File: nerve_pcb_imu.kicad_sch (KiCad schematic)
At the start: 15 parts, among them Y3 32k768

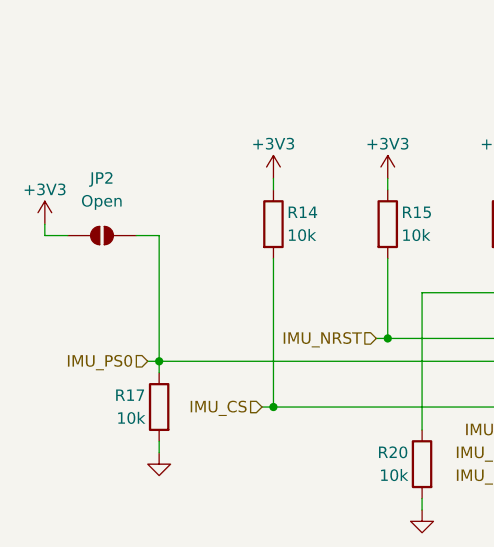
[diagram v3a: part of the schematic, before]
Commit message: Revert to 603 package sizes and add WIP PCB
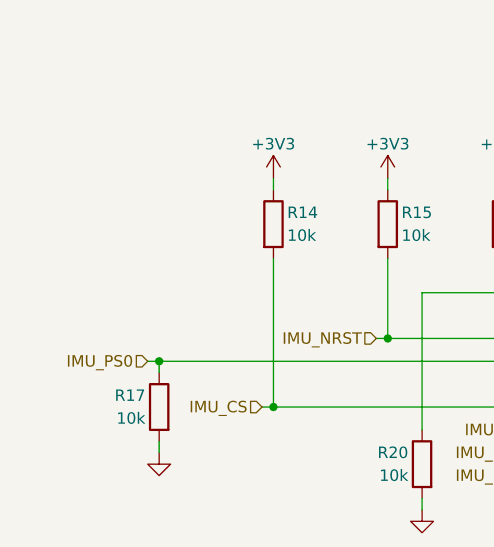
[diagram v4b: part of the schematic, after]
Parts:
- removed JP2: Open, Jumper:SolderJumper-2_P1.3mm_Open_TrianglePad1.0x1.5mm, symbol Jumper:SolderJumper_2_Open
- C16, C17, C20: footprint Capacitor_SMD:C_0402_1005Metric -> Capacitor_SMD:C_0603_1608Metric
- R14, R15, R16, R17, R18, R19, R20: footprint Resistor_SMD:R_0402_1005Metric -> Resistor_SMD:R_0603_1608Metric
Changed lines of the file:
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@@
-	(wire
-		(pts
-			(xy 95.25 88.9) (xy 95.25 102.87)
-		)
-		(stroke
-			(width 0)
-			(type default)
-		)
-	)
 	(wire
 		(pts
@@
 	(wire
 		(pts
-			(xy 82.55 87.63) (xy 82.55 88.9)
-		)
-		(stroke
-			(width 0)
-			(type default)
-		)
-	)
-	(wire
-		(pts
 			(xy 209.55 113.03) (xy 209.55 114.3)
 		)
@@
 	(wire
 		(pts
-			(xy 82.55 88.9) (xy 85.09 88.9)
-		)
-		(stroke
-			(width 0)
-			(type default)
-		)
-	)
-	(wire
-		(pts
 			(xy 107.95 91.44) (xy 107.95 107.95)
 		)
@@
 		(pts
 			(xy 203.2 124.46) (xy 209.55 124.46)
-		)
-		(stroke
-			(width 0)
-			(type default)
-		)
-	)
-	(wire
-		(pts
-			(xy 92.71 88.9) (xy 95.25 88.9)
 		)
 		(stroke
@@
 	)
 	(symbol
-		(lib_id "power:+3V3")
-		(at 82.55 87.63 0)
-		(unit 1)
-		(exclude_from_sim no)
-		(in_bom yes)
-		(on_board yes)
-		(dnp no)
-		(property "Reference" "#PWR063"
-			(at 82.55 91.44 0)
-			(effects
-				(font
-					(size 1.27 1.27)
-				)
-				(hide yes)
-			)
-		)
-		(property "Value" "+3V3"
-			(at 82.55 83.82 0)
-			(effects
-				(font
-					(size 1.27 1.27)
-				)
-			)
-		)
-		(property "Footprint" ""
-			(at 82.55 87.63 0)
-			(effects
-				(font
-					(size 1.27 1.27)
-				)
-				(hide yes)
-			)
-		)
-		(property "Datasheet" ""
-			(at 82.55 87.63 0)
-			(effects
-				(font
-					(size 1.27 1.27)
-				)
-				(hide yes)
-			)
-		)
-		(property "Description" "Power symbol creates a global label with name \"+3V3\""
-			(at 82.55 87.63 0)
-			(effects
-				(font
-					(size 1.27 1.27)
-				)
-				(hide yes)
-			)
-		)
-		(pin "1"
-		)
-		(instances
-			(project "nerve_pcb"
-				(path "/c0277862-b3f2-4e0e-986f-34702f0543f0/1178a2c5-f6af-4893-bc81-c8b9cb81f032"
-					(reference "#PWR063")
-					(unit 1)
-				)
-			)
-		)
-	)
-	(symbol
 		(lib_id "Device:C")
 		(at 166.37 76.2 0)
@@
 			)
 		)
-		(property "Footprint" "Capacitor_SMD:C_0402_1005Metric"
+		(property "Footprint" "Capacitor_SMD:C_0603_1608Metric"
 			(at 167.3352 80.01 0)
 			(effects
@@
 			)
 		)
-		(property "Footprint" "Capacitor_SMD:C_0402_1005Metric"
+		(property "Footprint" "Capacitor_SMD:C_0603_1608Metric"
 			(at 154.6352 133.35 0)
 			(effects
@@
 			)
 		)
-		(property "Footprint" "Resistor_SMD:R_0402_1005Metric"
+		(property "Footprint" "Resistor_SMD:R_0603_1608Metric"
 			(at 207.772 109.22 90)
 			(effects
@@
 			)
 		)
-		(property "Footprint" "Capacitor_SMD:C_0402_1005Metric"
+		(property "Footprint" "Capacitor_SMD:C_0603_1608Metric"
 			(at 180.0352 80.01 0)
 			(effects
@@
 	)
 	(symbol
-		(lib_id "Jumper:SolderJumper_2_Open")
-		(at 88.9 88.9 0)
-		(unit 1)
-		(exclude_from_sim yes)
-		(in_bom no)
-		(on_board yes)
-		(dnp no)
-		(fields_autoplaced yes)
-		(property "Reference" "JP2"
-			(at 88.9 82.55 0)
-			(effects
-				(font
-					(size 1.27 1.27)
-				)
-			)
-		)
-		(property "Value" "Open"
-			(at 88.9 85.09 0)
-			(effects
-				(font
-					(size 1.27 1.27)
-				)
-			)
-		)
-		(property "Footprint" "Jumper:SolderJumper-2_P1.3mm_Open_TrianglePad1.0x1.5mm"
-			(at 88.9 88.9 0)
-			(effects
-				(font
-					(size 1.27 1.27)
-				)
-				(hide yes)
-			)
-		)
-		(property "Datasheet" "~"
-			(at 88.9 88.9 0)
-			(effects
-				(font
-					(size 1.27 1.27)
-				)
-				(hide yes)
-			)
-		)
-		(property "Description" "Solder Jumper, 2-pole, open"
-			(at 88.9 88.9 0)
-			(effects
-				(font
-					(size 1.27 1.27)
-				)
-				(hide yes)
-			)
-		)
-		(pin "1"
-		)
-		(pin "2"
-		)
-		(instances
-			(project ""
-				(path "/c0277862-b3f2-4e0e-986f-34702f0543f0/1178a2c5-f6af-4893-bc81-c8b9cb81f032"
-					(reference "JP2")
-					(unit 1)
-				)
-			)
-		)
-	)
-	(symbol
 		(lib_id "Device:R")
 		(at 95.25 107.95 0)
@@
 			)
 		)
-		(property "Footprint" "Resistor_SMD:R_0402_1005Metric"
+		(property "Footprint" "Resistor_SMD:R_0603_1608Metric"
 			(at 97.028 107.95 90)
 			(effects
@@
 			)
 		)
-		(property "Footprint" "Resistor_SMD:R_0402_1005Metric"
+		(property "Footprint" "Resistor_SMD:R_0603_1608Metric"
 			(at 126.238 114.3 90)
 			(effects
@@
 			)
 		)
-		(property "Footprint" "Resistor_SMD:R_0402_1005Metric"
+		(property "Footprint" "Resistor_SMD:R_0603_1608Metric"
 			(at 118.872 87.63 90)
 			(effects
@@
 			)
 		)
-		(property "Footprint" "Resistor_SMD:R_0402_1005Metric"
+		(property "Footprint" "Resistor_SMD:R_0603_1608Metric"
 			(at 106.172 87.63 90)
 			(effects
@@
 			)
 		)
-		(property "Footprint" "Resistor_SMD:R_0402_1005Metric"
+		(property "Footprint" "Resistor_SMD:R_0603_1608Metric"
 			(at 131.572 87.63 90)
 			(effects
@@
 			)
 		)
-		(property "Footprint" "Resistor_SMD:R_0402_1005Metric"
+		(property "Footprint" "Resistor_SMD:R_0603_1608Metric"
 			(at 195.072 109.22 90)
 			(effects

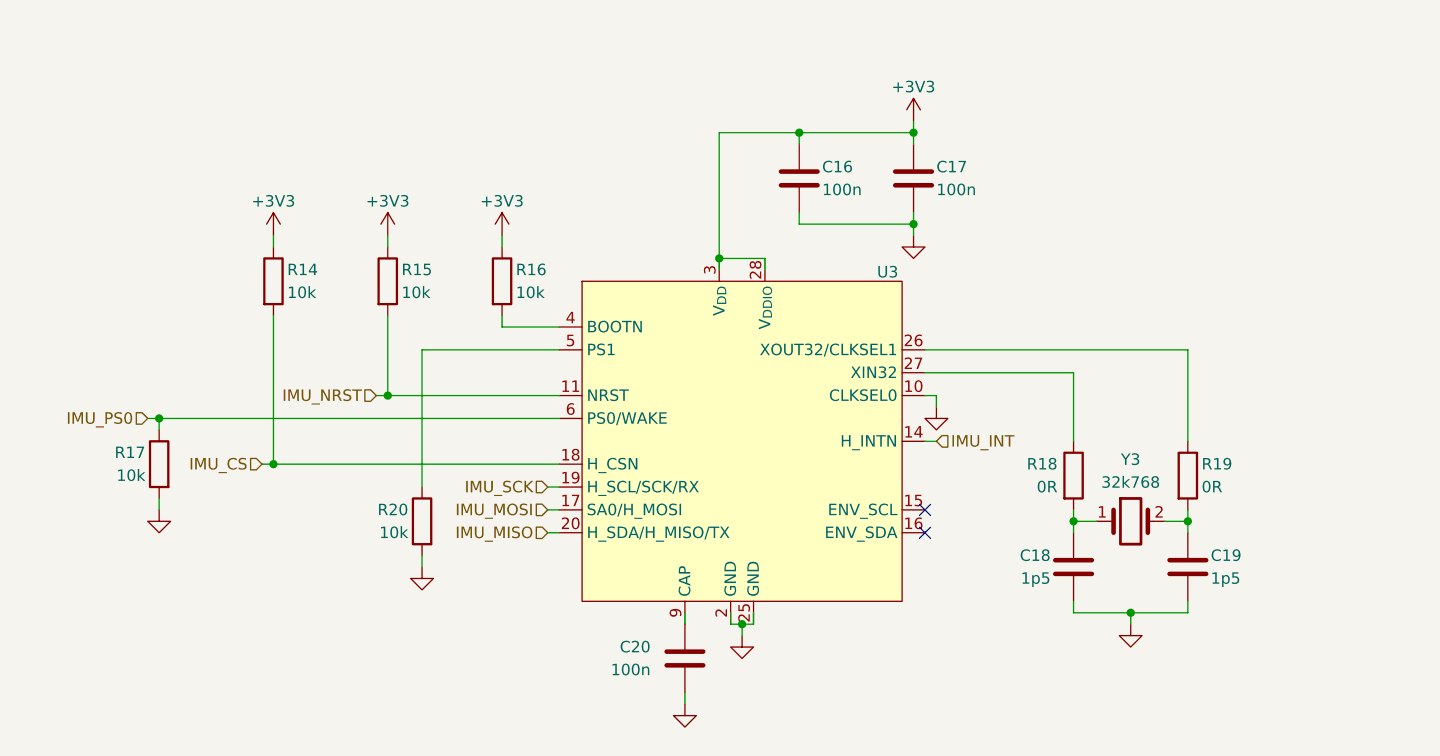
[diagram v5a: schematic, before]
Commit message: Clean up schematics and ensure PCB parity
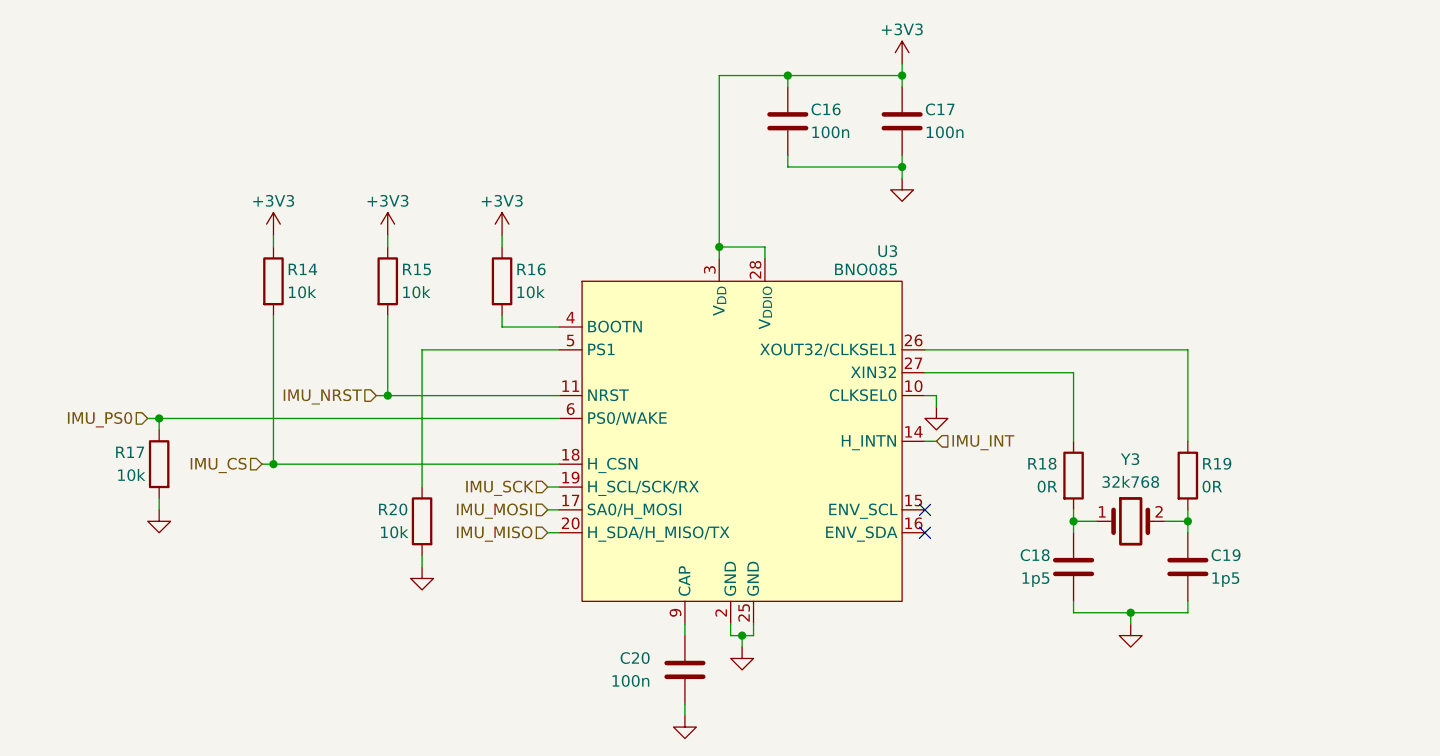
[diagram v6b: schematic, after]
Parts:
- U3: value ~ -> BNO085
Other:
- moved on the sheet: C16, C17, C20

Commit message: Cleanup Vbatt circuit and fix silkscreen
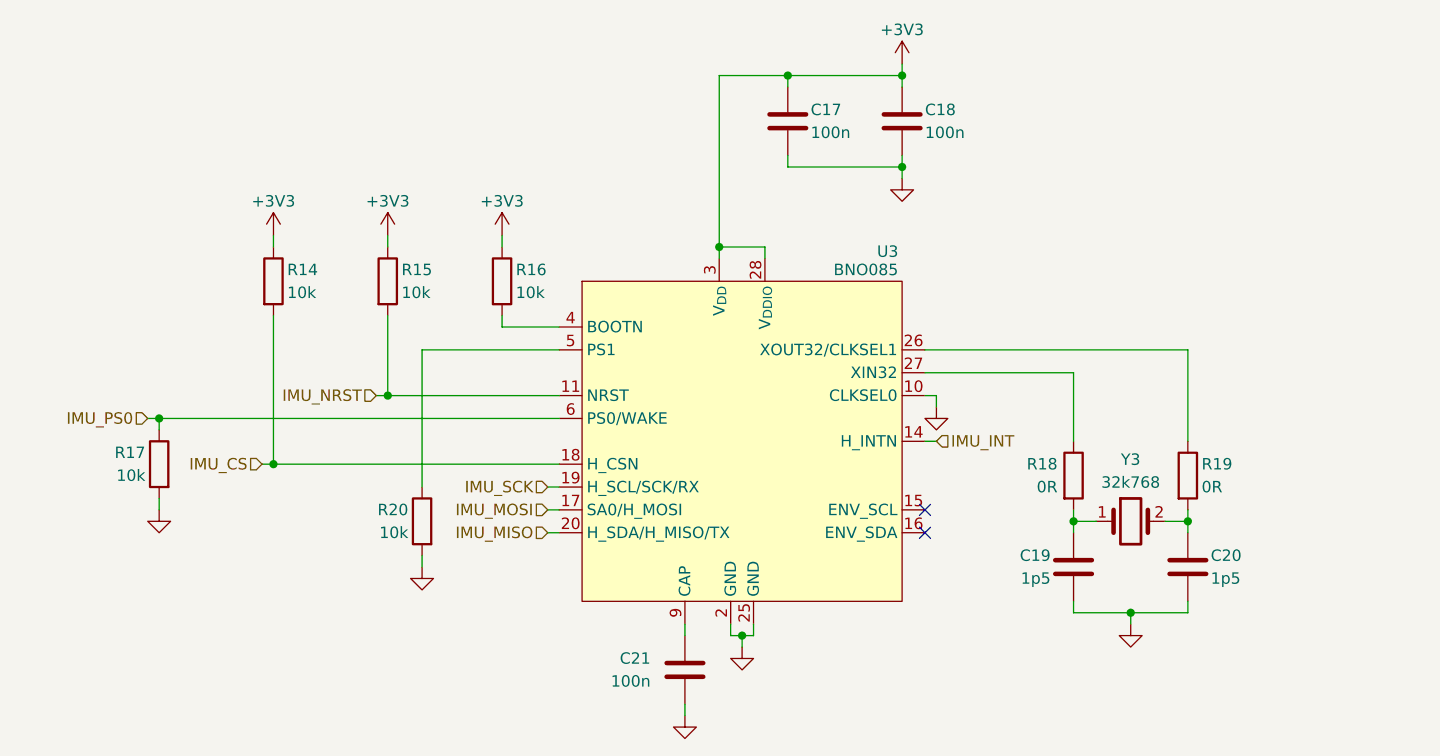
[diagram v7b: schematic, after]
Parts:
- renumbered C16 to C17, C17 to C18, C18 to C19, C19 to C20, C20 to C21
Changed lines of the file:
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@@
 		(on_board yes)
 		(dnp no)
-		(property "Reference" "C16"
+		(property "Reference" "C17"
 			(at 167.64 68.58 0)
 			(effects
@@
 			(project "nerve_pcb"
 				(path "/c0277862-b3f2-4e0e-986f-34702f0543f0/1178a2c5-f6af-4893-bc81-c8b9cb81f032"
-					(reference "C16")
+					(reference "C17")
 					(unit 1)
 				)
@@
 		(on_board yes)
 		(dnp no)
-		(property "Reference" "C19"
+		(property "Reference" "C20"
 			(at 212.09 118.11 0)
 			(effects
@@
 			(project "nerve_pcb"
 				(path "/c0277862-b3f2-4e0e-986f-34702f0543f0/1178a2c5-f6af-4893-bc81-c8b9cb81f032"
-					(reference "C19")
+					(reference "C20")
 					(unit 1)
 				)
@@
 		(dnp no)
 		(fields_autoplaced yes)
-		(property "Reference" "#PWR068"
+		(property "Reference" "#PWR070"
 			(at 153.67 142.24 0)
 			(effects
@@
 			(project "nerve_pcb"
 				(path "/c0277862-b3f2-4e0e-986f-34702f0543f0/1178a2c5-f6af-4893-bc81-c8b9cb81f032"
-					(reference "#PWR068")
+					(reference "#PWR070")
 					(unit 1)
 				)
@@
 		(on_board yes)
 		(dnp no)
-		(property "Reference" "C20"
+		(property "Reference" "C21"
 			(at 149.86 129.5399 0)
 			(effects
@@
 			(project ""
 				(path "/c0277862-b3f2-4e0e-986f-34702f0543f0/1178a2c5-f6af-4893-bc81-c8b9cb81f032"
-					(reference "C20")
+					(reference "C21")
 					(unit 1)
 				)
@@
 		(dnp no)
 		(fields_autoplaced yes)
-		(property "Reference" "#PWR065"
+		(property "Reference" "#PWR067"
 			(at 124.46 125.73 0)
 			(effects
@@
 			(project "nerve_pcb"
 				(path "/c0277862-b3f2-4e0e-986f-34702f0543f0/1178a2c5-f6af-4893-bc81-c8b9cb81f032"
-					(reference "#PWR065")
+					(reference "#PWR067")
 					(unit 1)
 				)
@@
 		(dnp no)
 		(fields_autoplaced yes)
-		(property "Reference" "#PWR064"
+		(property "Reference" "#PWR066"
 			(at 95.25 119.38 0)
 			(effects
@@
 			(project "nerve_pcb"
 				(path "/c0277862-b3f2-4e0e-986f-34702f0543f0/1178a2c5-f6af-4893-bc81-c8b9cb81f032"
-					(reference "#PWR064")
+					(reference "#PWR066")
 					(unit 1)
 				)
@@
 		(on_board yes)
 		(dnp no)
-		(property "Reference" "C17"
+		(property "Reference" "C18"
 			(at 180.34 68.58 0)
 			(effects
@@
 			(project "nerve_pcb"
 				(path "/c0277862-b3f2-4e0e-986f-34702f0543f0/1178a2c5-f6af-4893-bc81-c8b9cb81f032"
-					(reference "C17")
+					(reference "C18")
 					(unit 1)
 				)
@@
 		(on_board yes)
 		(dnp no)
-		(property "Reference" "C18"
+		(property "Reference" "C19"
 			(at 194.31 118.11 0)
 			(effects
@@
 			(project "nerve_pcb"
 				(path "/c0277862-b3f2-4e0e-986f-34702f0543f0/1178a2c5-f6af-4893-bc81-c8b9cb81f032"
-					(reference "C18")
+					(reference "C19")
 					(unit 1)
 				)
@@
 		(on_board yes)
 		(dnp no)
-		(property "Reference" "#PWR061"
+		(property "Reference" "#PWR063"
 			(at 120.65 86.36 0)
 			(effects
@@
 			(project "nerve_pcb"
 				(path "/c0277862-b3f2-4e0e-986f-34702f0543f0/1178a2c5-f6af-4893-bc81-c8b9cb81f032"
-					(reference "#PWR061")
+					(reference "#PWR063")
 					(unit 1)
 				)
@@
 		(dnp no)
 		(fields_autoplaced yes)
-		(property "Reference" "#PWR067"
+		(property "Reference" "#PWR069"
 			(at 160.02 134.62 0)
 			(effects
@@
 			(project "nerve_pcb"
 				(path "/c0277862-b3f2-4e0e-986f-34702f0543f0/1178a2c5-f6af-4893-bc81-c8b9cb81f032"
-					(reference "#PWR067")
+					(reference "#PWR069")
 					(unit 1)
 				)
@@
 		(dnp no)
 		(fields_autoplaced yes)
-		(property "Reference" "#PWR059"
+		(property "Reference" "#PWR061"
 			(at 177.8 82.55 0)
 			(effects
@@
 			(project "nerve_pcb"
 				(path "/c0277862-b3f2-4e0e-986f-34702f0543f0/1178a2c5-f6af-4893-bc81-c8b9cb81f032"
-					(reference "#PWR059")
+					(reference "#PWR061")
 					(unit 1)
 				)
@@
 		(on_board yes)
 		(dnp no)
-		(property "Reference" "#PWR062"
+		(property "Reference" "#PWR064"
 			(at 133.35 86.36 0)
 			(effects
@@
 			(project "nerve_pcb"
 				(path "/c0277862-b3f2-4e0e-986f-34702f0543f0/1178a2c5-f6af-4893-bc81-c8b9cb81f032"
-					(reference "#PWR062")
+					(reference "#PWR064")
 					(unit 1)
 				)
@@
 		(dnp no)
 		(fields_autoplaced yes)
-		(property "Reference" "#PWR066"
+		(property "Reference" "#PWR068"
 			(at 203.2 132.08 0)
 			(effects
@@
 			(project "nerve_pcb"
 				(path "/c0277862-b3f2-4e0e-986f-34702f0543f0/1178a2c5-f6af-4893-bc81-c8b9cb81f032"
-					(reference "#PWR066")
+					(reference "#PWR068")
 					(unit 1)
 				)
@@
 		(dnp no)
 		(fields_autoplaced yes)
-		(property "Reference" "#PWR063"
+		(property "Reference" "#PWR065"
 			(at 181.61 107.95 0)
 			(effects
@@
 			(project "nerve_pcb"
 				(path "/c0277862-b3f2-4e0e-986f-34702f0543f0/1178a2c5-f6af-4893-bc81-c8b9cb81f032"
-					(reference "#PWR063")
+					(reference "#PWR065")
 					(unit 1)
 				)
@@
 		(on_board yes)
 		(dnp no)
-		(property "Reference" "#PWR060"
+		(property "Reference" "#PWR062"
 			(at 107.95 86.36 0)
 			(effects
@@
 			(project "nerve_pcb"
 				(path "/c0277862-b3f2-4e0e-986f-34702f0543f0/1178a2c5-f6af-4893-bc81-c8b9cb81f032"
-					(reference "#PWR060")
+					(reference "#PWR062")
 					(unit 1)
 				)
@@
 		(on_board yes)
 		(dnp no)
-		(property "Reference" "#PWR058"
+		(property "Reference" "#PWR060"
 			(at 177.8 67.31 0)
 			(effects
@@
 			(project "nerve_pcb"
 				(path "/c0277862-b3f2-4e0e-986f-34702f0543f0/1178a2c5-f6af-4893-bc81-c8b9cb81f032"
-					(reference "#PWR058")
-					(unit 1)
-				)
+					(reference "#PWR060")
+					(unit 1)
+				)

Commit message: Schematic corrections
- Add decoupling caps for sensor ICs
- Fix clock circuits
- Add BNO085 clock jumper
- Minor cleanup
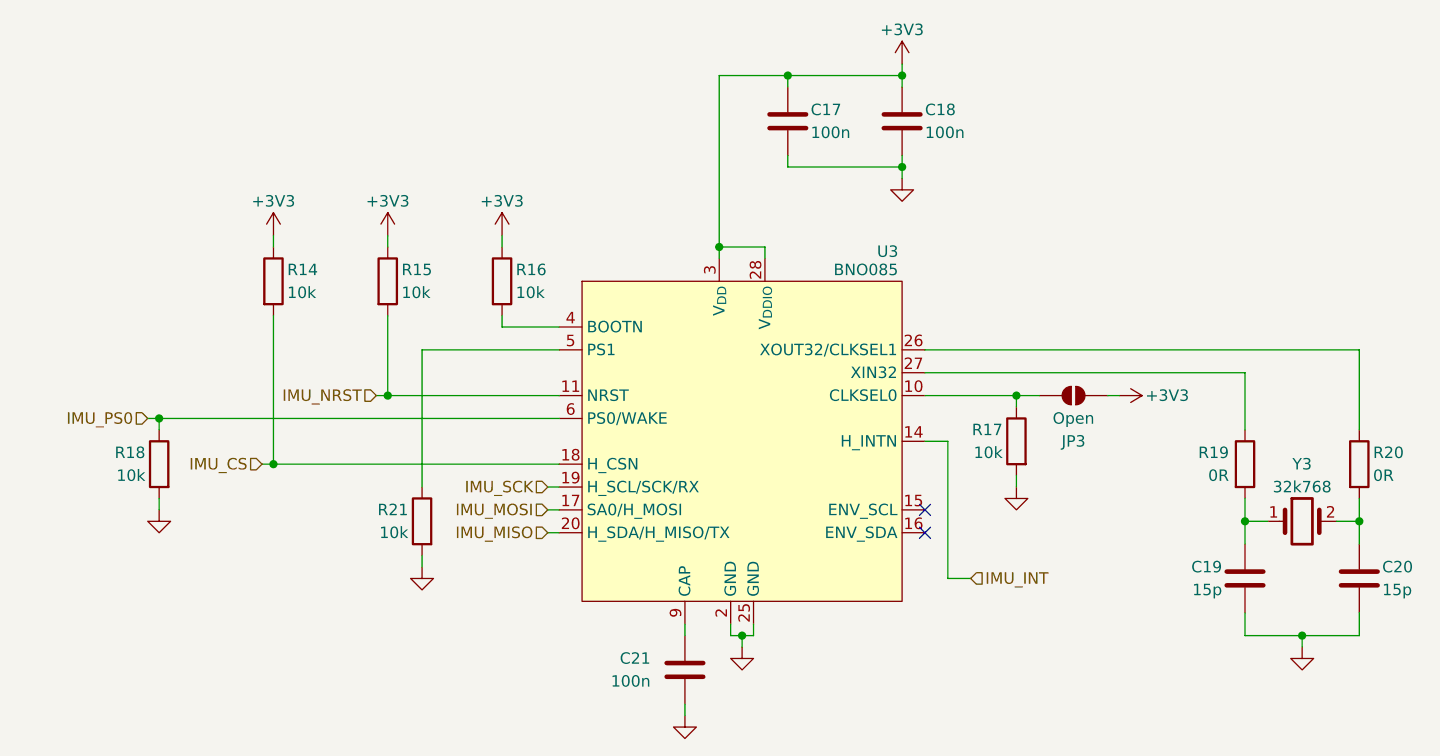
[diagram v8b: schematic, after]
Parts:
- removed Y3: 32k768, common:xtal_abs25-32.768khz-6-t, symbol common:abs25-32.768khz-6-t
- added JP3: Open, Jumper:SolderJumper-2_P1.3mm_Open_TrianglePad1.0x1.5mm, symbol Jumper:SolderJumper_2_Open
- added R17: 10k, Resistor_SMD:R_0603_1608Metric, symbol Device:R
- added Y3: 32k768, common:ecs_ecx-34r, symbol common:ecs-_327-12_5-34r-c-tr_32k768hz
- C19, C20: value 1p5 -> 15p
- renumbered R17 to R18, R18 to R19, R19 to R20, R20 to R21
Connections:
- net +3V3: now also JP3.2 (B)
- net GND: now also R17.2; no longer U3.10 (CLKSEL0)
- net at C20.1, R20.2: now also Y3.2
- net at C19.1, R19.2: now also Y3.1
- new net: JP3.1 (A), R17.1, U3.10 (CLKSEL0)
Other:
- moved on the sheet: C19, C20, R19, R20
